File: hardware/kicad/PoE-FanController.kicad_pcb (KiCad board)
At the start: 2 copper layers, 56 x 78 mm, 26 parts, among them J2 FAN1, J3 FAN2, J4 FAN3, J5 FAN4, J8 Waveshare_ESP32P4POEETH, U1 LM2587-12

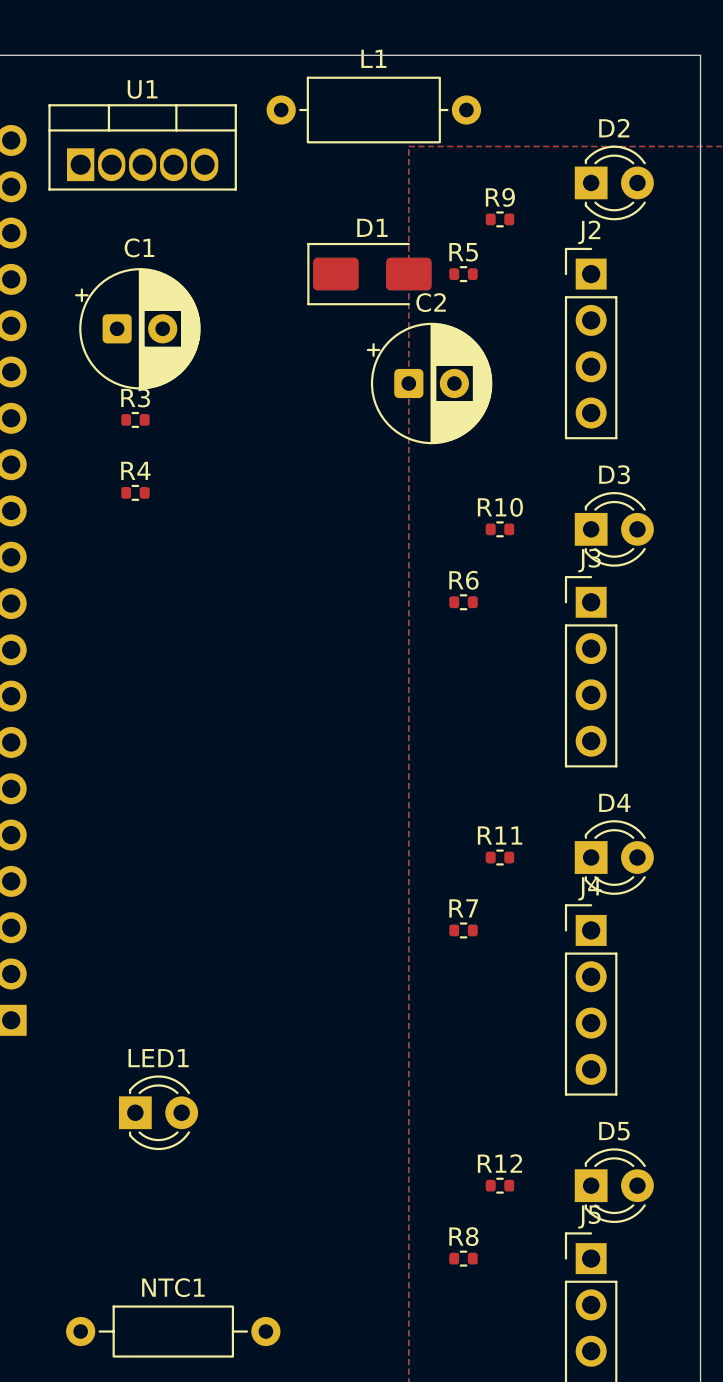
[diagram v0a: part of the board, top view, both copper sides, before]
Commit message: hw: replace all 0402 resistors with 0805 for hand-solderability (issue #90)
- R3, R4, R5-R8, R9-R12: footprint changed from R_0402_1005Metric to R_0805_2012Metric
- All pad geometries, courtyards, silkscreen updated to 0805 dimensions
- BOM: Yageo MPN updated to RC0805FR-07xxx equivalents
- D1 repositioned to (48, 2.5) to maintain clearance from L1 pad 2 at (43.16, 3)
  and from fan indicator LEDs above fan headers
- DRC: 0 real errors, 0 courtyard overlaps, 63 unconnected (routing pending)
- ERC: 0 errors

Co-authored-by: Copilot <223556219+Copilot@users.noreply.github.com>
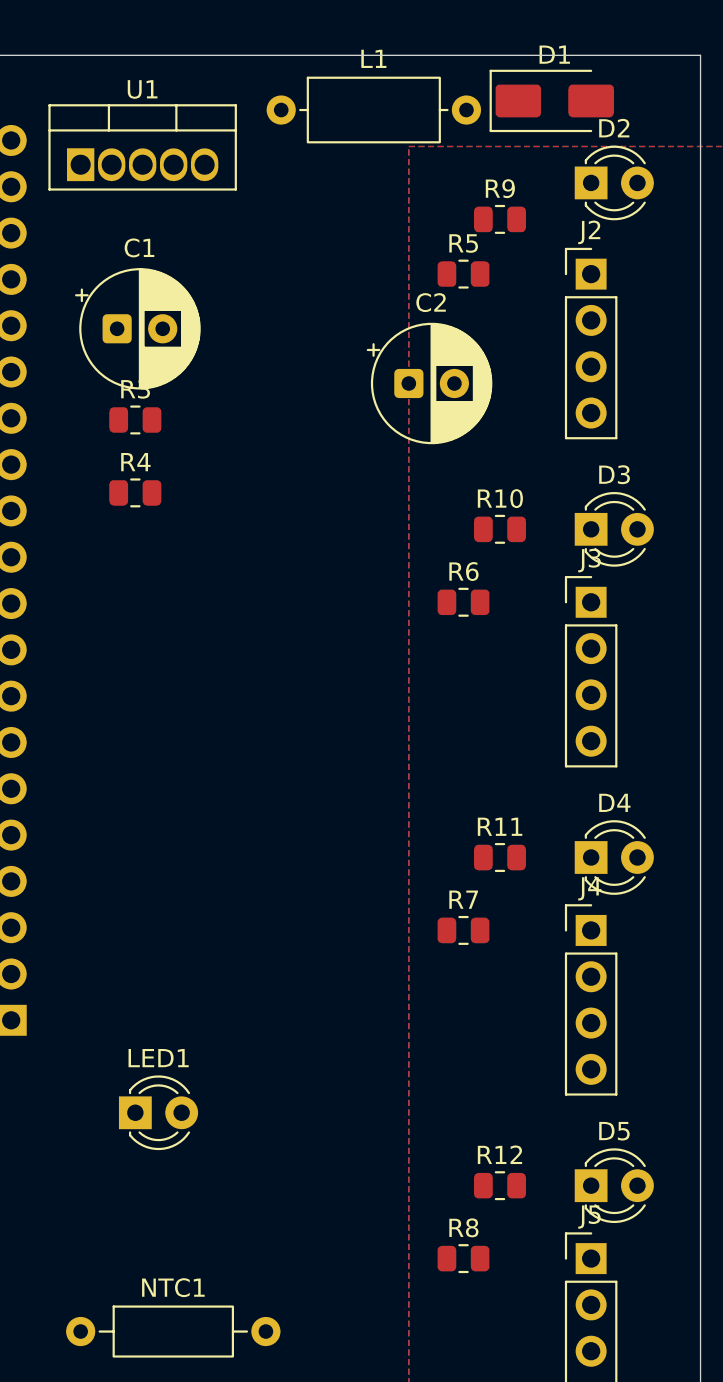
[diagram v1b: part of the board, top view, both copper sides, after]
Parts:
- R10, R11, R12, R9: value R_0402_1005Metric -> Resistor_SMD:R_0805_2012Metric; footprint R_0402_1005Metric -> Resistor_SMD:R_0805_2012Metric
- R3, R4, R5, R6, R7, R8: footprint Resistor_SMD:R_0402_1005Metric -> Resistor_SMD:R_0805_2012Metric
- moved D1 13.8 mm to (48.0, 2.50)

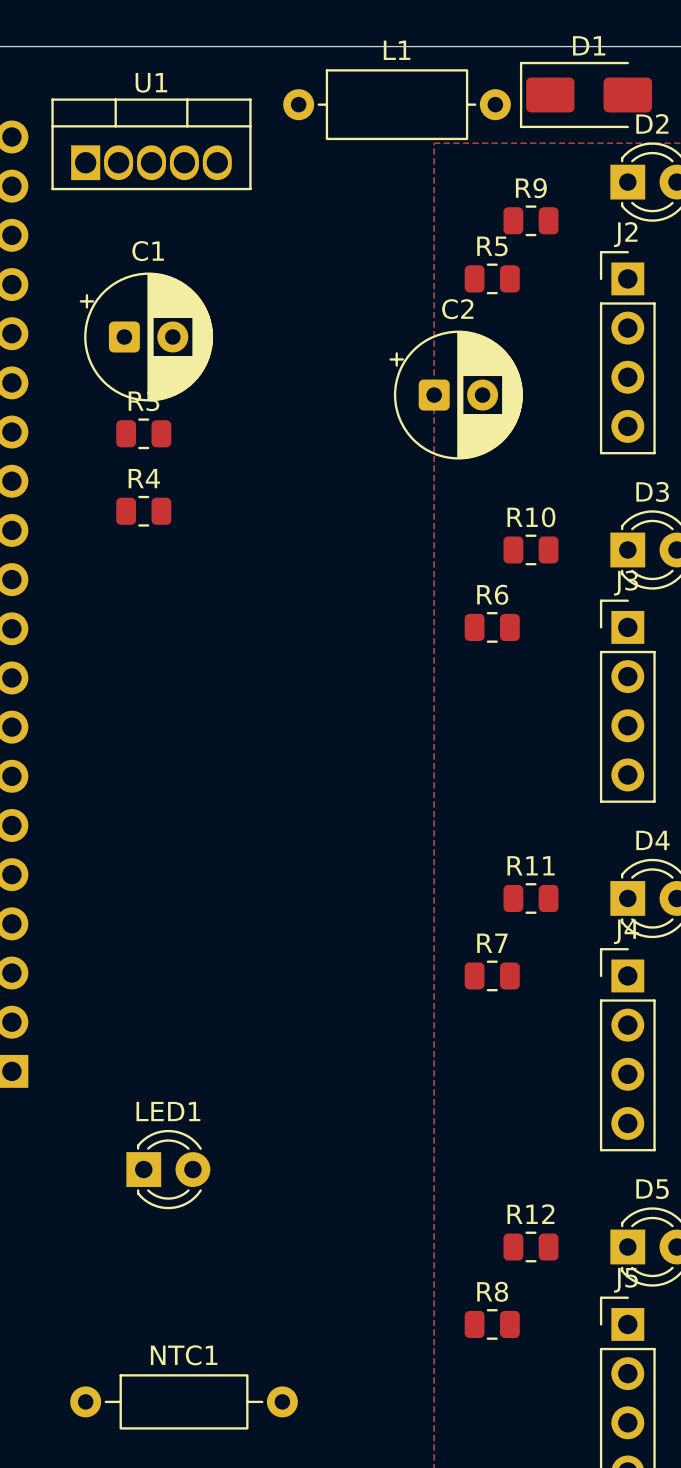
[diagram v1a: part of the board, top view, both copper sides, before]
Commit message: hw: replace all SMD resistors with P7.62mm THT axial (issue #90)
- All 10 resistors (R3, R4, R5-R8, R9-R12) changed from 0805 SMD to
  Resistor_THT:R_Axial_DIN0207_L6.3mm_D2.5mm_P7.62mm_Horizontal
  (1/4W axial THT — hand-solderable without microscope)
- BOM: Yageo MFR-25FBF52 series (1/4W 1% axial THT)
- PCB footprint anchors adjusted to keep pad 2 clear of fan headers/LEDs:
    R5-R8 (TACH pull-ups):  anchor (35, 12/30/48/66), pad2 at X=42.62
    R9-R12 (LED current):   anchor (36, 7/25/43/61),  pad2 at X=43.62
    R3, R4: anchor unchanged at (25, 20) and (25, 24)
- DRC: 0 real errors, 0 courtyard overlaps, 63 unconnected (routing pending)

Co-authored-by: Copilot <223556219+Copilot@users.noreply.github.com>
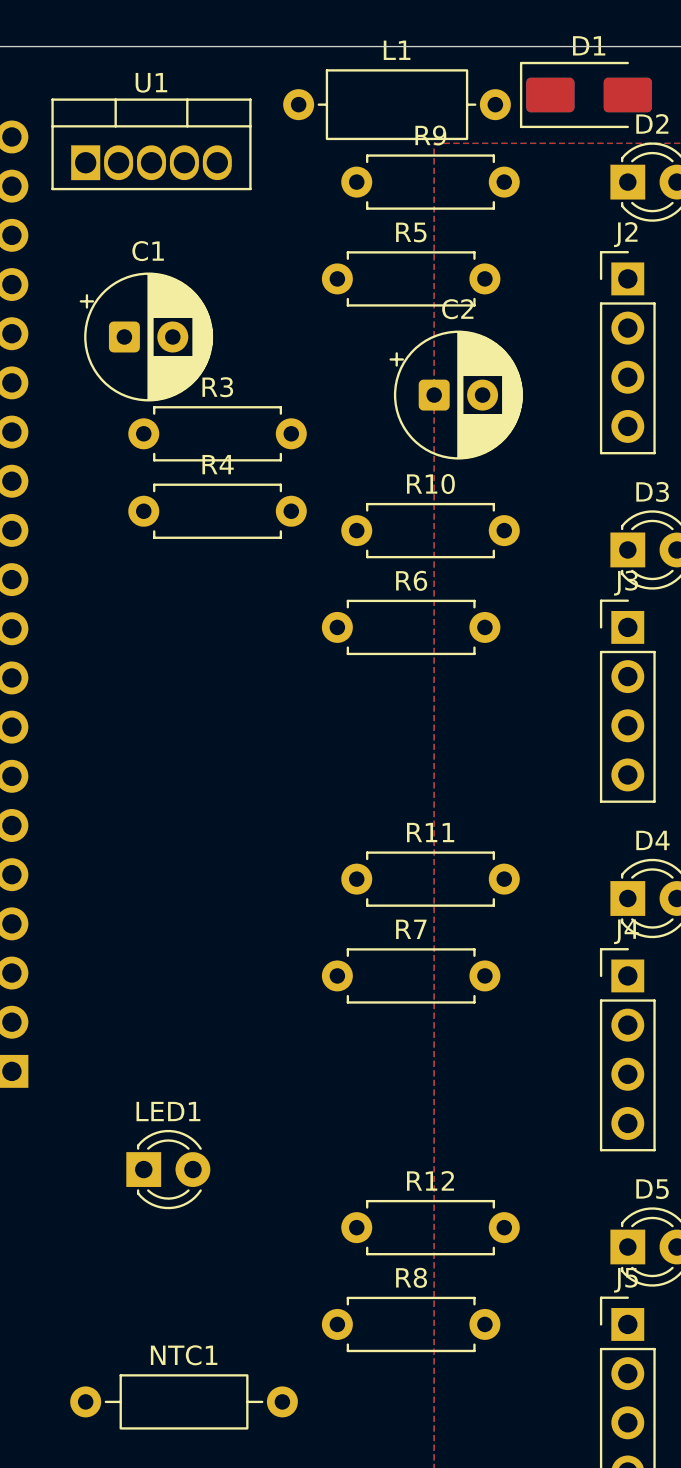
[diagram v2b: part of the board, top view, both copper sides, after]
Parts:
- R10, R11, R12, R9: value Resistor_SMD:R_0805_2012Metric -> 1k; footprint Resistor_SMD:R_0805_2012Metric -> R_Axial_DIN0207_L6.3mm_D2.5mm_P7.62mm_Horizontal
- R3, R4, R5, R6, R7, R8: footprint Resistor_SMD:R_0805_2012Metric -> R_Axial_DIN0207_L6.3mm_D2.5mm_P7.62mm_Horizontal
- moved R9 9.22 mm to (36.0, 7.00)
- moved R10 9.06 mm to (36.0, 25.0)
- moved R11 9.06 mm to (36.0, 43.0)
- moved R12 9.06 mm to (36.0, 61.0)
- moved R5 8.00 mm to (35.0, 12.0)
- moved R6 8.00 mm to (35.0, 30.0)
- moved R7 8.00 mm to (35.0, 48.0)
- moved R8 8.00 mm to (35.0, 66.0)

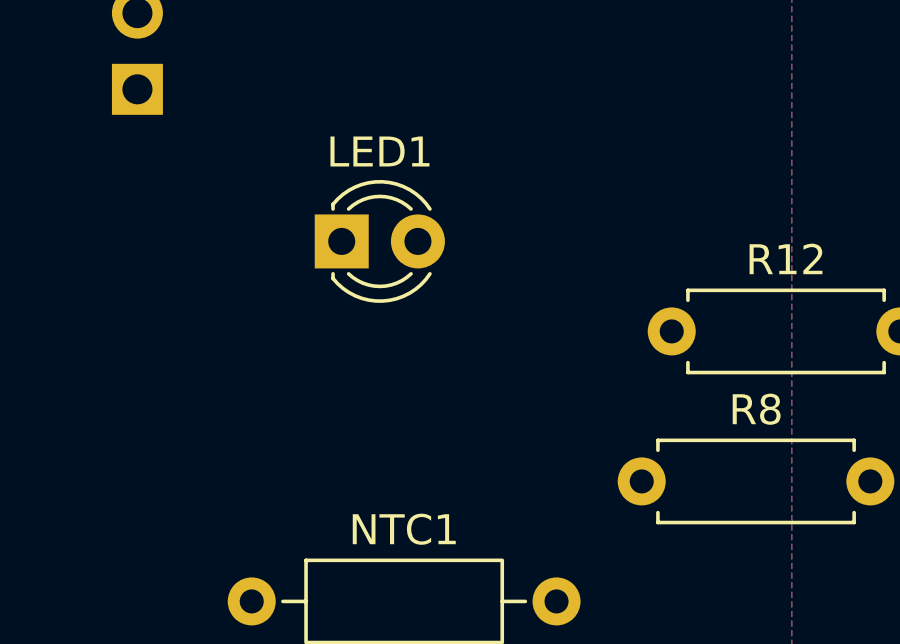
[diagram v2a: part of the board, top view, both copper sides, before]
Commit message: hw+fw: add orange prog/OTA LED (issue #89)
Hardware:
- R13 (330Ω THT, P7.62mm) placed at PCB (25, 64)
- LED2 (orange 3mm THT, Wurth 150060AS75000) placed at PCB (31, 58)
  next to LED1 (green status LED)
- Circuit: PROG_LED → R13 → PROG_LED_A → LED2 anode → GND
- J8 pin 22 (GPIO15) wired to PROG_LED net (was NC)
- ERC: 0 errors · DRC: 0 real errors · 0 courtyard overlaps
- BOM updated with R13 and LED2 entries

Firmware:
- pins.h: add PROG_LED_PIN (GPIO15)
- ota.cpp: add ota_init() to configure GPIO15; LED2 flickers on each
  OTA chunk write, holds HIGH on success, LOW on error
- main.cpp: call ota_init() in setup()

Co-authored-by: Copilot <223556219+Copilot@users.noreply.github.com>
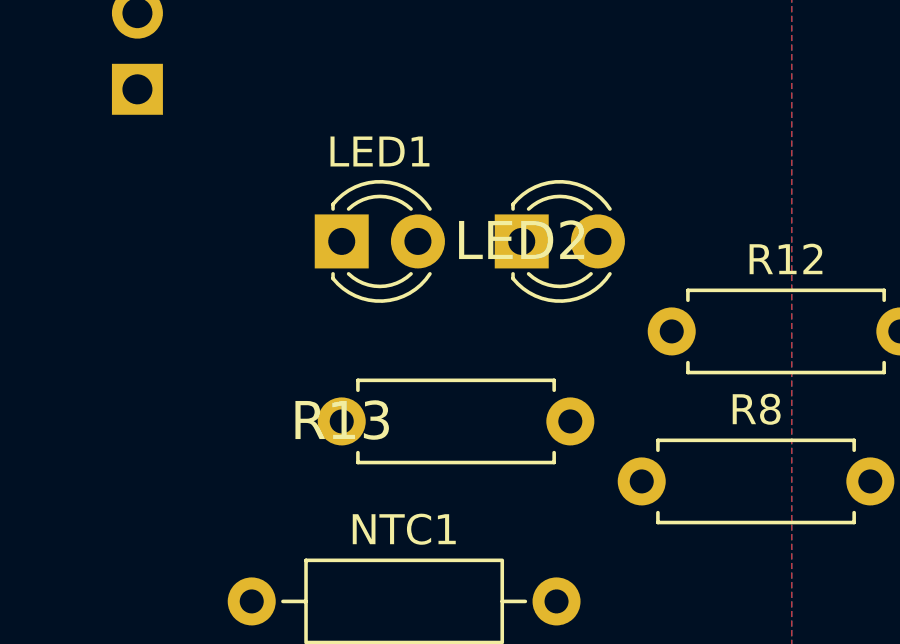
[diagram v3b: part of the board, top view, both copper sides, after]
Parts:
- added LED2: LED_ORANGE, LED_D3.0mm, F.Cu at (31.0, 58.0)
- added R13: 330R, R_Axial_DIN0207_L6.3mm_D2.5mm_P7.62mm_Horizontal, F.Cu at (25.0, 64.0)

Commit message: hw(pcb): place NV-Home-Lab logo in bottom-left PCB corner (issue #87)
- Generated NV-Home-Lab-Logo.kicad_mod from nv-home-lab-logo.kicad_sym
  (scaled 86.70 mm symbol → 10 mm footprint, 301 filled polygons on F.SilkS)
- Placed at PCB position (8, 73) in the bottom-left corner
  (clear of J8 connector which ends at Y~53, and all other components)
- DRC: 0 real errors, 0 courtyard overlaps
  (silk_overlap/silk_edge_clearance warnings are cosmetic for a logo element)

Co-authored-by: Copilot <223556219+Copilot@users.noreply.github.com>
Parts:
- added #G1: NV-Home-Lab-Logo, NV-Home-Lab-Logo, F.Cu at (8.00, 73.0)

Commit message: hw(pcb): place NV-Home-Lab logo in bottom-left PCB corner (issue #87)
- nv-home-lab-logo.kicad_mod added to Custom.pretty footprint library
  (provided by user; bitmap2component output, 429 polygons, corrected
  from F.Cu to F.SilkS so no copper DRC errors)
- Logo scaled 86.70mm → 20mm and placed at PCB (12, 67) in bottom-left corner
  (clear of J8 which ends at Y≈53; 2mm margins from board edges)
- DRC: 0 real errors, 0 courtyard overlaps
  (silk_overlap/silk_over_copper/silk_edge_clearance warnings are cosmetic)

Co-authored-by: Copilot <223556219+Copilot@users.noreply.github.com>
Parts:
- #G1: value NV-Home-Lab-Logo -> LOGO; footprint NV-Home-Lab-Logo -> LOGO; moved to F.SilkS
- moved #G1 73.4 mm to (0.00, 0.00)

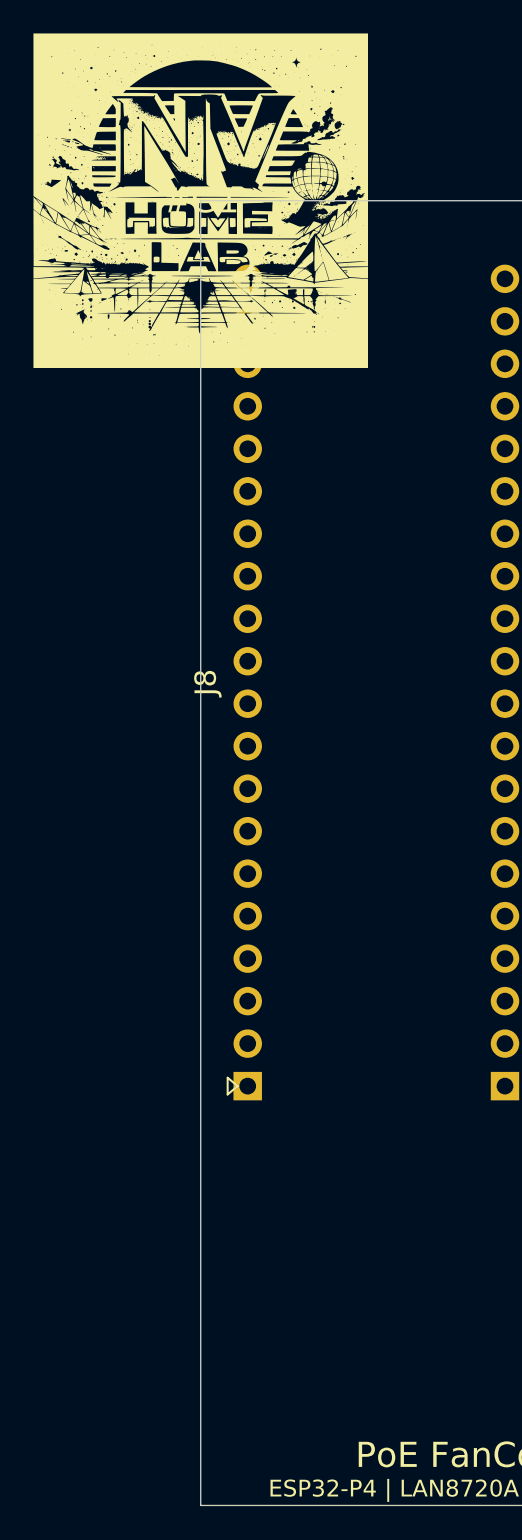
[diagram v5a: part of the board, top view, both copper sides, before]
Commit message: hw(pcb): inverted 12mm NV-Home-Lab logo in bottom-left corner (issue #87)
- Logo scaled to 12mm (from 86.70mm native), placed at PCB (7, 71)
  Spans X: 1-13mm, Y: 65-77mm — 1mm margins from left and bottom edges
  Clear of all components (NTC1@X=22, J8 ends at Y=53)
- Inverted rendering: solid white 12.4mm bounding box with logo shapes
  subtracted (shapely boolean difference → 1207 separate fp_poly pieces)
  White background + dark logo features = high contrast on any board colour
- All polygons on F.SilkS (no copper conflicts)
- DRC: 0 real errors, 0 courtyard overlaps
  (silk_overlap/silk_over_copper/silk_edge_clearance warnings are cosmetic)

Co-authored-by: Copilot <223556219+Copilot@users.noreply.github.com>
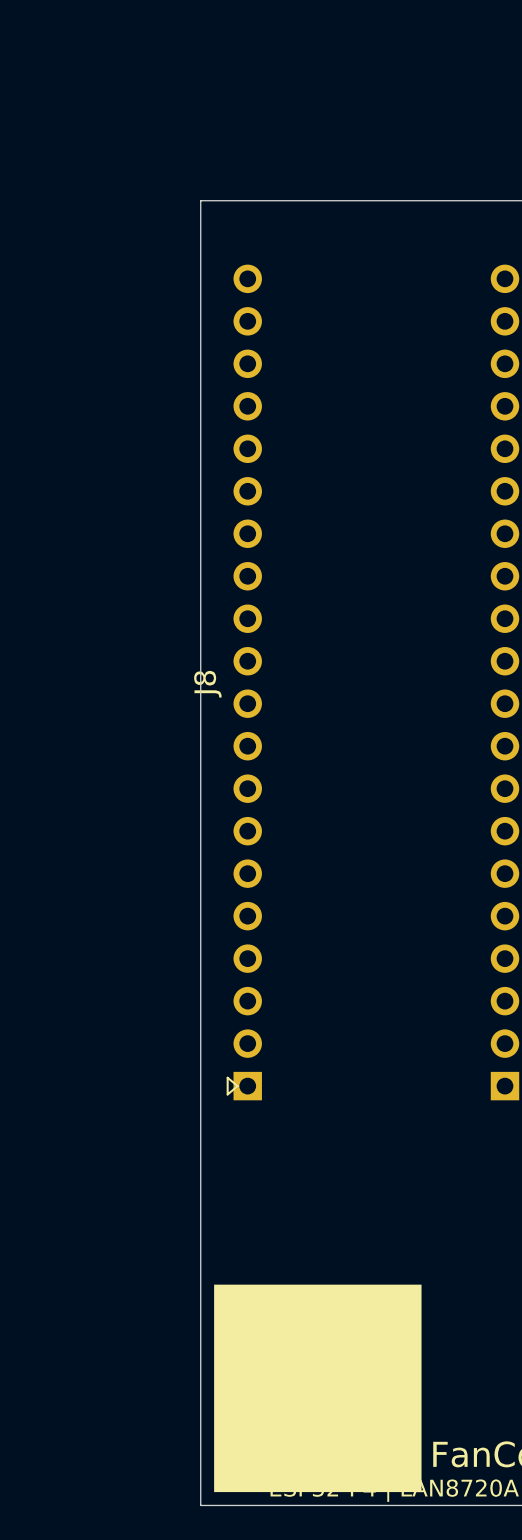
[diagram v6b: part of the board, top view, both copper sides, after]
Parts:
- #G1: value LOGO -> NV-Home-Lab-Logo; footprint LOGO -> Custom:NV-Home-Lab-Logo
- moved #G1 71.3 mm to (7.00, 71.0)
